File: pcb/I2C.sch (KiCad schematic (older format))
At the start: 12 parts, among them U10 PCF8523TK, Y1 ABS06-107-32.768KHZ-T

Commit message: rtc placement
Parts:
- C24: footprint Capacitors_THT:CP_Radial_D6.3mm_P2.50mm -> Capacitor_THT:CP_Radial_D6.3mm_P2.50mm
- D7: footprint Diodes_SMD:D_SOD-523 -> Diode_SMD:D_SOD-523
- R13: footprint MATRIX_SMD:R_0402_NoSilk -> Resistor_SMD:R_0402_1005Metric
- Y1: footprint MATRIX_SMD:ABS06-107 -> SMD:ABS06-107
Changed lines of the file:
@@
 $Descr A4 11693 8268
 encoding utf-8
-Sheet 9 9
+Sheet 7 9
 Title ""
 Date ""
@@
 F 0 "C24" H 5075 2650 50  0000 L CNN
 F 1 "JUWT1105MCD" H 4925 2550 39  0000 L CNN
-F 2 "Capacitors_THT:CP_Radial_D6.3mm_P2.50mm" H 5350 2650 50  0001 C CNN
+F 2 "Capacitor_THT:CP_Radial_D6.3mm_P2.50mm" H 5350 2650 50  0001 C CNN
 F 3 "~" H 5350 2650 50  0001 C CNN
 	1    5350 2650
@@
 F 0 "R13" V 4929 2401 50  0000 L CNN
 F 1 "100" V 5020 2401 50  0000 L CNN
-F 2 "MATRIX_SMD:R_0402_NoSilk" H 5125 2475 50  0001 C CNN
+F 2 "Resistor_SMD:R_0402_1005Metric" H 5125 2475 50  0001 C CNN
 F 3 "~" H 5125 2475 50  0001 C CNN
 	1    5125 2475
@@
 F 0 "D7" H 4750 2375 50  0000 L CNN
 F 1 " 1SS389,L3F" H 4650 2575 39  0000 L CNN
-F 2 "Diodes_SMD:D_SOD-523" V 4825 2475 50  0001 C CNN
+F 2 "Diode_SMD:D_SOD-523" V 4825 2475 50  0001 C CNN
 F 3 "~" V 4825 2475 50  0001 C CNN
 	1    4825 2475
@@
 F 0 "Y1" H 5500 2076 39  0000 C CNN
 F 1 "ABS06-107-32.768KHZ-T" H 5500 2001 39  0000 C CNN
-F 2 "MATRIX_SMD:ABS06-107" H 5500 1875 50  0001 C CNN
+F 2 "SMD:ABS06-107" H 5500 1875 50  0001 C CNN
 F 3 "~" H 5500 1875 50  0001 C CNN
 	1    5500 1875

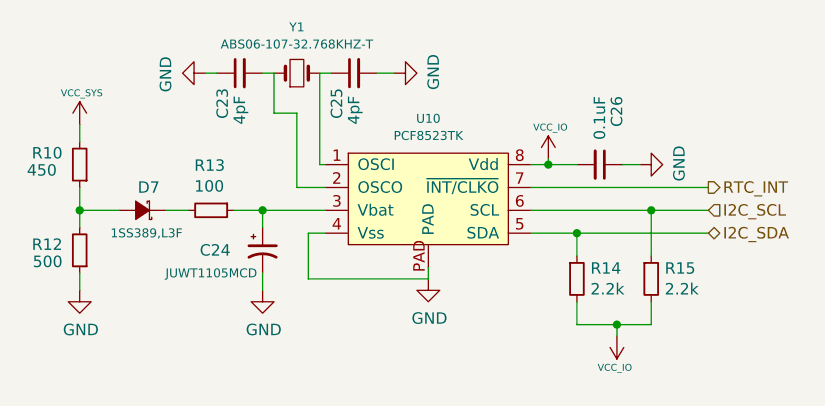
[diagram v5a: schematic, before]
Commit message: 3v3_ice removed
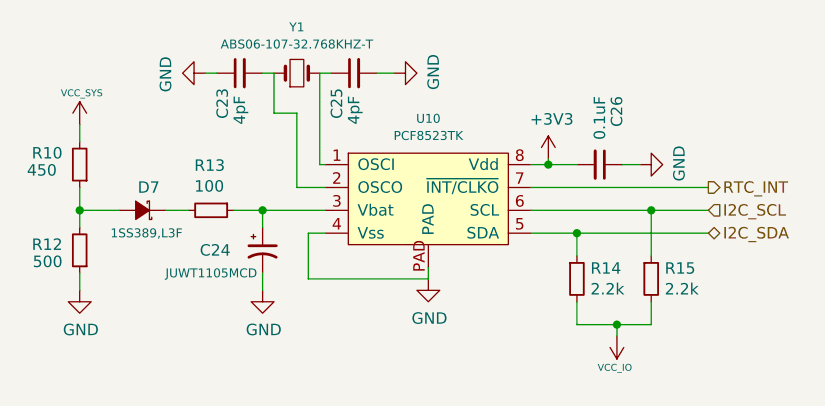
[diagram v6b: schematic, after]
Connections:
- net VCC_IO: no longer C26.2, U10.8 (Vdd)
- new net +3V3: C26.2, U10.8 (Vdd)
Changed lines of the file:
@@
 EESchema Schematic File Version 4
-LIBS:keep_breathing_ctrl-cache
 EELAYER 30 0
 EELAYER END
@@
 	1    0    0    -1
 $EndComp
-$Comp
-L ventilator-PowerSymbols:VCC_IO #PWR0133
-U 1 1 5B76DDB5
-P 6600 2250
-F 0 "#PWR0133" H 6600 2210 30  0001 C CNN
-F 1 "VCC_IO" H 6609 2388 30  0000 C CNN
-F 2 "" H 6600 2250 60  0000 C CNN
-F 3 "" H 6600 2250 60  0000 C CNN
-	1    6600 2250
-	1    0    0    -1
-$EndComp
 Wire Wire Line
 	6600 2250 6600 2275
@@
 Wire Wire Line
 	6900 2975 7050 2975
+$Comp
+L power:+3V3 #PWR?
+U 1 1 5EA9F31F
+P 6600 2250
+F 0 "#PWR?" H 6600 2100 50  0001 C CNN
+F 1 "+3V3" H 6615 2423 50  0000 C CNN
+F 2 "" H 6600 2250 50  0001 C CNN
+F 3 "" H 6600 2250 50  0001 C CNN
+	1    6600 2250
+	1    0    0    -1
+$EndComp
 $EndSCHEMATC

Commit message: fixing i2c sensors
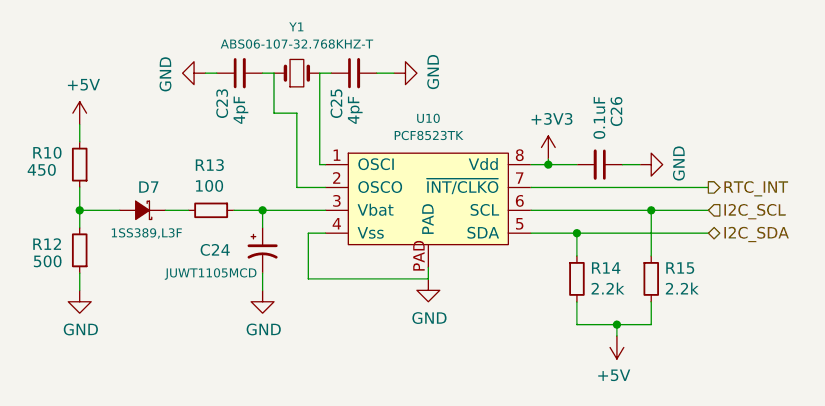
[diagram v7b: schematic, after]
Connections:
- net VCC_SYS is gone; now on net +5V: R10.2
- net VCC_IO renamed +5V
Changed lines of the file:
@@
 Wire Wire Line
 	4550 2475 4550 2550
-$Comp
-L ventilator-PowerSymbols:VCC_SYS #PWR0159
-U 1 1 5B776E96
-P 4550 2100
-F 0 "#PWR0159" H 4550 2060 30  0001 C CNN
-F 1 "VCC_SYS" H 4559 2238 30  0000 C CNN
-F 2 "" H 4550 2100 60  0000 C CNN
-F 3 "" H 4550 2100 60  0000 C CNN
-	1    4550 2100
-	1    0    0    -1
-$EndComp
 Wire Wire Line
 	4550 2100 4550 2175
@@
 	7050 2475 7300 2475
 Connection ~ 7050 2475
-$Comp
-L ventilator-PowerSymbols:VCC_IO #PWR0137
-U 1 1 5B77ADCB
-P 6900 3025
-F 0 "#PWR0137" H 6900 2985 30  0001 C CNN
-F 1 "VCC_IO" H 6909 3163 30  0000 C CNN
-F 2 "" H 6900 3025 60  0000 C CNN
-F 3 "" H 6900 3025 60  0000 C CNN
-	1    6900 3025
-	-1   0    0    1
-$EndComp
 Wire Wire Line
 	6725 2875 6725 2975
@@
 	6900 2975 7050 2975
 $Comp
-L power:+3V3 #PWR?
+L power:+3V3 #PWR0245
 U 1 1 5EA9F31F
 P 6600 2250
-F 0 "#PWR?" H 6600 2100 50  0001 C CNN
+F 0 "#PWR0245" H 6600 2100 50  0001 C CNN
 F 1 "+3V3" H 6615 2423 50  0000 C CNN
 F 2 "" H 6600 2250 50  0001 C CNN
@@
 	1    0    0    -1
 $EndComp
+$Comp
+L power:+5V #PWR0246
+U 1 1 5EA1D9D7
+P 4550 2100
+F 0 "#PWR0246" H 4550 1950 50  0001 C CNN
+F 1 "+5V" H 4565 2273 50  0000 C CNN
+F 2 "" H 4550 2100 50  0001 C CNN
+F 3 "" H 4550 2100 50  0001 C CNN
+	1    4550 2100
+	1    0    0    -1
+$EndComp
+$Comp
+L power:+5V #PWR0247
+U 1 1 5EA2221B
+P 6900 3025
+F 0 "#PWR0247" H 6900 2875 50  0001 C CNN
+F 1 "+5V" H 6915 3198 50  0000 C CNN
+F 2 "" H 6900 3025 50  0001 C CNN
+F 3 "" H 6900 3025 50  0001 C CNN
+	1    6900 3025
+	-1   0    0    1
+$EndComp
 $EndSCHEMATC

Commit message: routing...
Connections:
- net +3V3: now also R14.2, R15.2
- net +5V: no longer R14.2, R15.2
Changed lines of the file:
@@
 $EndComp
 $Comp
-L power:+5V #PWR0247
-U 1 1 5EA2221B
+L power:+3V3 #PWR?
+U 1 1 5EA2635D
 P 6900 3025
-F 0 "#PWR0247" H 6900 2875 50  0001 C CNN
-F 1 "+5V" H 6915 3198 50  0000 C CNN
+F 0 "#PWR?" H 6900 2875 50  0001 C CNN
+F 1 "+3V3" H 6915 3198 50  0000 C CNN
 F 2 "" H 6900 3025 50  0001 C CNN
 F 3 "" H 6900 3025 50  0001 C CNN
